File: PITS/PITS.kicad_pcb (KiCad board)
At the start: 2 copper layers, 65 x 30 mm, 55 parts, among them P1 CONN_02X20, P10 I2C, P11 I2C, P12 I2C, P13 I2C, P14 BATT, P2 BNC, P3 BNC, P4 BNC, P5 BNC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

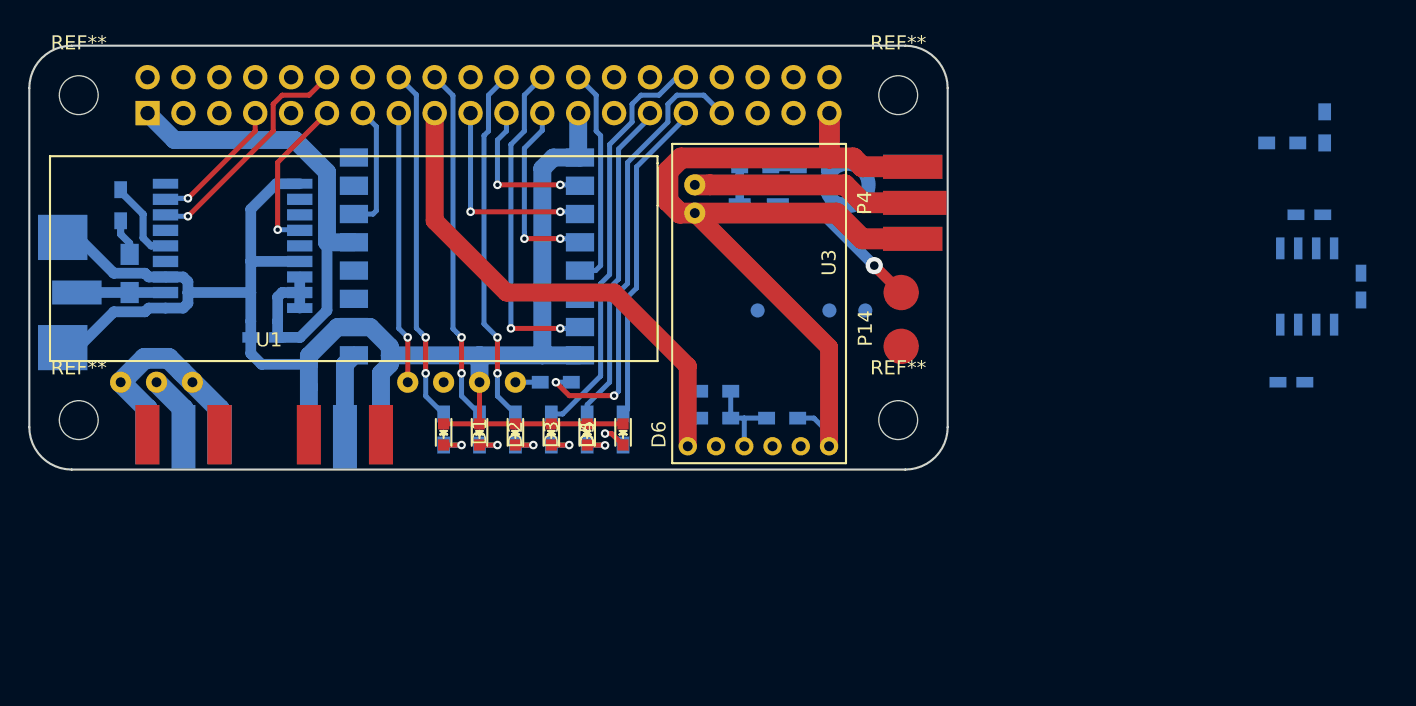
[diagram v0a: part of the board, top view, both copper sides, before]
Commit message: ADC, BME280 and power switch
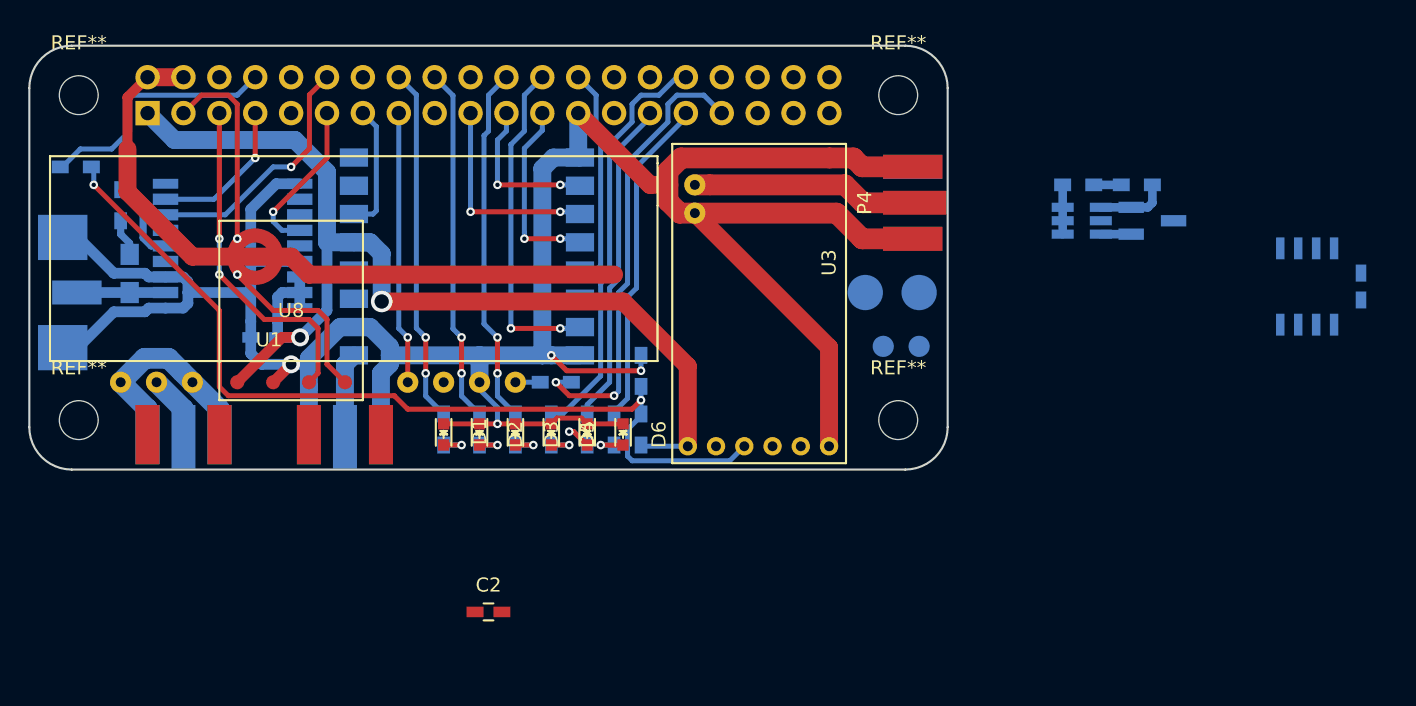
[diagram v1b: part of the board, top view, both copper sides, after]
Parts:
- removed C4: 100n, Capacitors_SMD:C_0603_HandSoldering
- removed R12, R13: 10k, Resistors_SMD:R_0603_HandSoldering
- added P6: Batt, Connectors:SMD_2_xsmall, B.Cu at (115.4, 70.3)
- C2, U8: moved to F.Cu
- P14: moved to B.Cu
- moved C2 64.5 mm to (87.5, 89.1)
- moved R3 48.0 mm to (58.3, 57.6)
- moved U8 44.7 mm to (69.7, 72.8), turned to 0 degrees
- moved Q1 22.9 mm to (134.5, 61.4)
- moved Q2 22.9 mm to (129.5, 61.4)
- moved R6 22.9 mm to (129.2, 58.9)
- moved R19 22.9 mm to (133.4, 58.9)
- moved R2 10.5 mm to (98.3, 72.0), turned to 90 degrees
- moved R4 5.31 mm to (98.3, 76.2), turned to 90 degrees
- moved P14 1.27 mm to (118.0, 66.5), turned to 180 degrees
- moved R23 0.64 mm to (96.4, 76.2)
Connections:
- C2 pad 2: GND -> Net-(C2-Pad2)
- P1 pad 2: +5V -> I_neg
- P1 pad 4: +5V -> I_neg
- P14 pad 1: +5V_PSU -> I_pos
- Q1 pad 1: +5V_PSU -> I_pos
- Q1 pad 3: +5V -> I_neg
- Q2 pad 5: +5V -> I_neg
- Q2 pad 6: +5V_PSU -> I_pos
- U1 pad 5: +5V -> I_neg
- U5 pad 3: +5V_PSU -> I_pos
- U7 pad 2: GND -> Net-(C2-Pad2)
- U7 pad 7: Iout -> I_pos
- U7 pad 8: GND -> I_neg
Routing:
- net /MTX2-TXD: track 6.44 -> 64.2 mm, vias 0 -> 2
- net I_neg: track 0.00 -> 48.1 mm
- net /GPIO2(SDA1): track 0.00 -> 29.3 mm, vias 0 -> 2
- net /GPIO3(SCL1): track 0.00 -> 24.1 mm, vias 0 -> 2
- net /GPIO14(TXD0): track 0.00 -> 17.8 mm
- net GND: track 201.4 -> 213.6 mm, vias 0 -> 4
- net +5V_PSU: track 11.0 -> 0.00 mm, vias 1 -> 0
- net +3V3: track 75.2 -> 81.4 mm, vias 0 -> 2
- net I_pos: track 0.00 -> 2.15 mm
- net /GPIO4: track 9.62 -> 10.7 mm
- net /GPIO18: track 16.7 -> 17.7 mm
- net /D6: track 3.37 -> 2.53 mm
- net /D5: track 2.55 -> 3.33 mm
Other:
- net class POWER: via_dia 1.2192 -> 1.524; via_drill 0.6096 -> 1.016

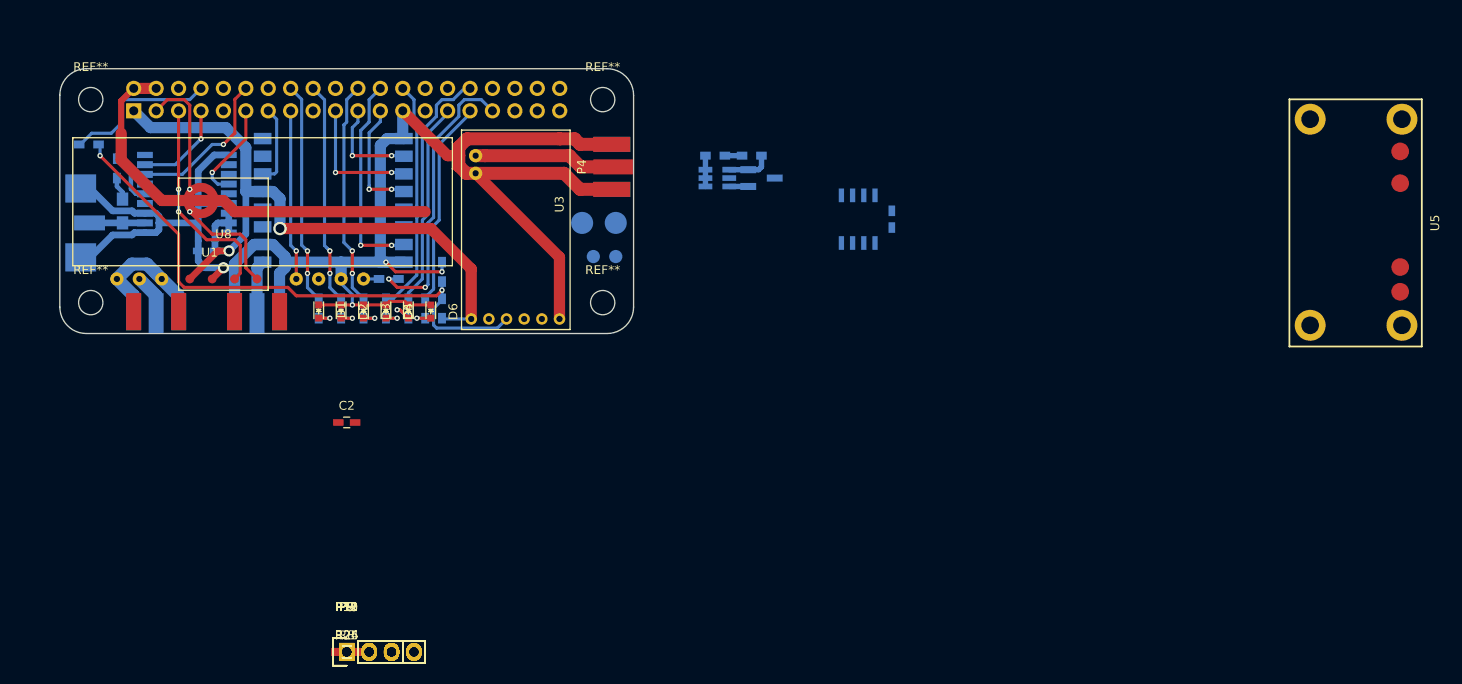
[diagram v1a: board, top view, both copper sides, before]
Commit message: Layout almost finished
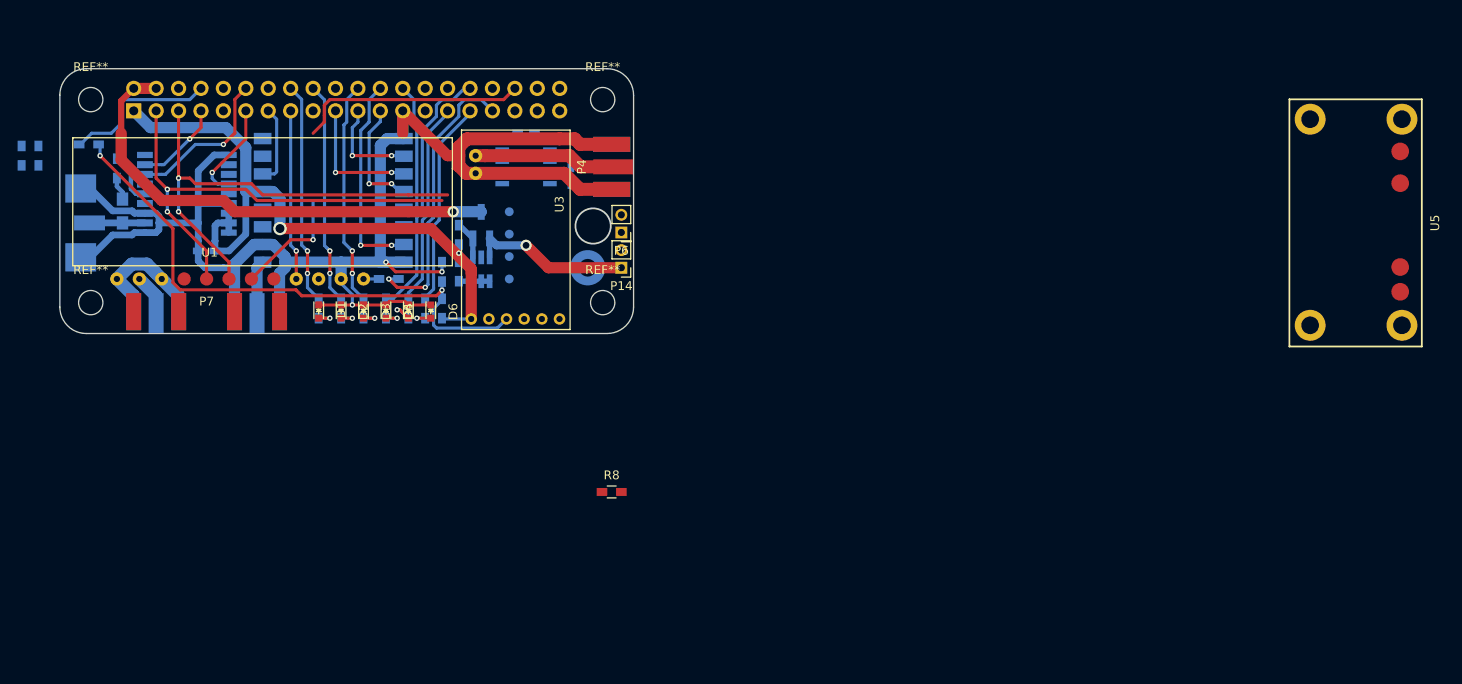
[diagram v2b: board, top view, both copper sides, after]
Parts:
- removed P10, P11, P12, P13: I2C, Socket_Strips:Socket_Strip_Straight_1x04
- removed P8, P9: 1-WIRE, Socket_Strips:Socket_Strip_Straight_1x03
- C2, R24, R25: moved to B.Cu
- P14: footprint Connectors:SMD_2_small -> Pin_Headers:Pin_Header_Straight_1x02_Pitch2.00mm; moved to F.Cu
- P6: footprint Connectors:SMD_2_xsmall -> Pin_Headers:Pin_Header_Straight_1x02_Pitch2.00mm; moved to F.Cu
- P7: value 1-WIRE -> SENSOR; footprint Socket_Strips:Socket_Strip_Straight_1x03 -> Connectors:SMD_5_xsmall
- U8: footprint RF_Modules:BME280 -> RF_Modules:BME280_edit; moved to B.Cu
- moved R24 67.2 mm to (50.7, 58.9), turned to 90 degrees
- moved R25 66.2 mm to (52.6, 58.9), turned to 90 degrees
- moved P7 46.1 mm to (69.1, 72.8)
- moved C1 42.6 mm to (107.8, 56.3), turned to 0 degrees
- moved U7 38.1 mm to (107.8, 60.1), turned to 0 degrees
- moved C2 37.8 mm to (112.9, 61.1), turned to 270 degrees
- moved U8 36.2 mm to (105.9, 72.8), turned to 90 degrees
- moved R8 35.1 mm to (117.5, 97.0)
- moved R19 34.4 mm to (100.2, 67.8), turned to 270 degrees
- moved Q1 32.2 mm to (102.7, 66.7), turned to 180 degrees
- moved R6 31.9 mm to (100.2, 72.0), turned to 90 degrees
- moved Q2 28.7 mm to (102.7, 71.7), turned to 90 degrees
- moved P14 5.12 mm to (118.6, 71.5)
- moved P6 4.19 mm to (118.6, 67.5), turned to 180 degrees
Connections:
- P7 pad 2: /GPIO4 -> /GPIO2(SDA1)
- P7 pad 3: GND -> /GPIO3(SCL1)
- R8 pad 2: /GPIO4 -> /GPIO16(CE2)
- U7 pad 1: Net-(C2-Pad1) -> I_neg
- U7 pad 2: Net-(C2-Pad2) -> I_pos
- U7 pad 7: I_pos -> Net-(C2-Pad1)
- U7 pad 8: I_neg -> Net-(C2-Pad2)
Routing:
- net /GPIO16(CE2): track 0.00 -> 39.4 mm, vias 0 -> 1
- net /GPIO3(SCL1): track 24.1 -> 52.7 mm
- net /GPIO2(SDA1): track 29.3 -> 53.1 mm
- net GND: track 213.6 -> 193.9 mm
- net I_pos: track 2.15 -> 18.5 mm, vias 0 -> 1
- net I_neg: track 48.1 -> 54.5 mm, vias 0 -> 1
- net +3V3: track 81.4 -> 75.6 mm, vias 2 -> 1
- net /GPIO4: track 10.7 -> 9.99 mm
- net Net-(Q1-Pad2): track 5.05 -> 4.36 mm

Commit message: Some cleanup
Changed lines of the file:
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@@
-    )
-  )
-  (module RF_Modules:MTX2 locked (layer F.Cu)
-    (at 101.605 58.35 270)
-    (fp_text reference U3 (at 6 -10 270) (layer F.SilkS)
-      (effects (font (size 1 1) (thickness 0.15)))
-    )
-    (fp_text value MTX2 (at 0 -10 270) (layer F.Fab)
-      (effects (font (size 1 1) (thickness 0.15)))
-    )
-    (fp_line (start -2.4 1.1) (end 20.2 1.1) (layer F.SilkS) (width 0.15))
-    (fp_line (start 20.2 1.1) (end 20.2 -11.2) (layer F.SilkS) (width 0.15))
-    (fp_line (start 20.2 -11.2) (end -2.4 -11.2) (layer F.SilkS) (width 0.15))
-    (fp_line (start -2.4 -11.2) (end -2.4 1.1) (layer F.SilkS) (width 0.15))
-    (pad 1 thru_hole circle (at 0.5 -0.5 270) (size 1.5 1.5) (drill 0.7) (layers *.Cu *.Mask)
-      (net 31 "Net-(P4-Pad1)"))
-    (pad 2 thru_hole circle (at 2.5 -0.5 270) (size 1.5 1.5) (drill 0.7) (layers *.Cu *.Mask)
-      (net 4 GND))
-    (pad 3 thru_hole circle (at 19 0 270) (size 1.3 1.3) (drill 0.7) (layers *.Cu *.Mask)
-      (net 1 +3V3))
-    (pad 4 thru_hole circle (at 19 -2 270) (size 1.3 1.3) (drill 0.7) (layers *.Cu *.Mask)
-      (net 60 "Net-(U3-Pad4)"))
-    (pad 5 thru_hole circle (at 19 -4 270) (size 1.3 1.3) (drill 0.7) (layers *.Cu *.Mask)
-      (net 42 /MTX2-TXD))
-    (pad 6 thru_hole circle (at 19 -6 270) (size 1.3 1.3) (drill 0.7) (layers *.Cu *.Mask)
-      (net 53 "Net-(U3-Pad6)"))
-    (pad 7 thru_hole circle (at 19 -8 270) (size 1.3 1.3) (drill 0.7) (layers *.Cu *.Mask)
-      (net 54 "Net-(U3-Pad7)"))
-    (pad 8 thru_hole circle (at 19 -10 270) (size 1.3 1.3) (drill 0.7) (layers *.Cu *.Mask)
-      (net 4 GND))
-    (model RF_Modules.3dshapes/MTX2.wrl
-      (at (xyz 0 0 0))
-      (scale (xyz 0.393700787 0.393700787 0.393700787))
-      (rotate (xyz 0 0 0))
     )
   )
@@
       (rotate (xyz 0 0 0))
     )
+  )
+  (module RF_Modules:MTX2 locked (layer F.Cu)
+    (at 101.605 58.35 270)
+    (fp_text reference U3 (at 6 -10 270) (layer F.SilkS)
+      (effects (font (size 1 1) (thickness 0.15)))
+    )
+    (fp_text value MTX2 (at 0 -10 270) (layer F.Fab)
+      (effects (font (size 1 1) (thickness 0.15)))
+    )
+    (fp_line (start -2.6 1.3) (end 20.4 1.3) (layer F.SilkS) (width 0.15))
+    (fp_line (start 20.4 1.3) (end 20.4 -11.4) (layer F.SilkS) (width 0.15))
+    (fp_line (start 20.4 -11.4) (end -2.6 -11.4) (layer F.SilkS) (width 0.15))
+    (fp_line (start -2.6 -11.4) (end -2.6 1.3) (layer F.SilkS) (width 0.15))
+    (pad 1 thru_hole circle (at 0.5 -0.5 270) (size 1.5 1.5) (drill 0.8) (layers *.Cu *.Mask)
+      (net 31 "Net-(P4-Pad1)"))
+    (pad 2 thru_hole circle (at 2.5 -0.5 270) (size 1.5 1.5) (drill 0.8) (layers *.Cu *.Mask)
+      (net 4 GND))
+    (pad 3 thru_hole circle (at 19 0 270) (size 1.3 1.3) (drill 0.8) (layers *.Cu *.Mask)
+      (net 1 +3V3))
+    (pad 4 thru_hole circle (at 19 -2 270) (size 1.3 1.3) (drill 0.8) (layers *.Cu *.Mask)
+      (net 60 "Net-(U3-Pad4)"))
+    (pad 5 thru_hole circle (at 19 -4 270) (size 1.3 1.3) (drill 0.8) (layers *.Cu *.Mask)
+      (net 42 /MTX2-TXD))
+    (pad 6 thru_hole circle (at 19 -6 270) (size 1.3 1.3) (drill 0.8) (layers *.Cu *.Mask)
+      (net 53 "Net-(U3-Pad6)"))
+    (pad 7 thru_hole circle (at 19 -8 270) (size 1.3 1.3) (drill 0.8) (layers *.Cu *.Mask)
+      (net 54 "Net-(U3-Pad7)"))
+    (pad 8 thru_hole circle (at 19 -10 270) (size 1.3 1.3) (drill 0.8) (layers *.Cu *.Mask)
+      (net 4 GND))
+    (model RF_Modules.3dshapes/MTX2.wrl
+      (at (xyz 0 0 0))
+      (scale (xyz 0.393700787 0.393700787 0.393700787))
+      (rotate (xyz 0 0 0))
+    )

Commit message: PCB save
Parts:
- moved U5 59.7 mm to (142.1, 65.2)
- moved R8 56.4 mm to (142.1, 46.1)
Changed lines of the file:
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@@
   )
   (module Resistors_SMD:R_0603_HandSoldering (layer F.Cu)
-    (at 117.515 96.95)
+    (at 142.11 46.15)
     (descr "Resistor SMD 0603, hand soldering")
     (tags "resistor 0603")
@@
     (model RF_Modules.3dshapes/HX1.wrl
       (at (xyz -0.19685 0.059055 0))
-      (scale (xyz 0.393701 0.393701 0.393701))
-      (rotate (xyz 0 0 0))
-    )
-  )
-  (module power:TPS61030 (layer F.Cu)
-    (at 201.8 66.47 90)
-    (fp_text reference U5 (at 0 9 90) (layer F.SilkS)
-      (effects (font (size 1 1) (thickness 0.15)))
-    )
-    (fp_text value TPS61030 (at 0 0 90) (layer F.Fab)
-      (effects (font (size 1 1) (thickness 0.15)))
-    )
-    (fp_line (start 14 7.5) (end -14 7.5) (layer F.SilkS) (width 0.2))
-    (fp_line (start 14 -7.5) (end 14 7.5) (layer F.SilkS) (width 0.2))
-    (fp_line (start -14 -7.5) (end 14 -7.5) (layer F.SilkS) (width 0.2))
-    (fp_line (start -14 7.5) (end -14 -7.5) (layer F.SilkS) (width 0.2))
-    (pad 1 smd circle (at -7.8 5.05 90) (size 2 2) (layers F.Cu F.Paste F.Mask)
-      (net 27 +BATT))
-    (pad 2 smd circle (at -5 5.05 90) (size 2 2) (layers F.Cu F.Paste F.Mask)
-      (net 4 GND))
-    (pad 2 smd circle (at 4.5 5.05 90) (size 2 2) (layers F.Cu F.Paste F.Mask)
-      (net 4 GND))
-    (pad 3 smd circle (at 8.1 5.05 90) (size 2 2) (layers F.Cu F.Paste F.Mask)
-      (net 65 I_pos))
-    (pad 4 thru_hole circle (at -11.6 5.25 90) (size 3.5 3.5) (drill 2) (layers B.Cu B.Mask))
-    (pad 4 thru_hole circle (at -11.6 -5.15 90) (size 3.5 3.5) (drill 2) (layers B.Cu B.Mask))
-    (pad 4 thru_hole circle (at 11.75 -5.15 90) (size 3.5 3.5) (drill 2) (layers B.Cu B.Mask))
-    (pad 4 thru_hole circle (at 11.75 5.25 90) (size 3.5 3.5) (drill 2) (layers B.Cu B.Mask))
-    (model power.3dshapes/TPS61030-1.wrl
-      (at (xyz -0.551181 -0.295276 0.28))
       (scale (xyz 0.393701 0.393701 0.393701))
       (rotate (xyz 0 0 0))
@@
       (rotate (xyz 0 0 0))
     )
+  )
+  (module power:TPS61030 (layer F.Cu)
+    (at 142.11 65.2 90)
+    (fp_text reference U5 (at 0 9 90) (layer F.SilkS)
+      (effects (font (size 1 1) (thickness 0.15)))
+    )
+    (fp_text value TPS61030 (at 0 0 90) (layer F.Fab)
+      (effects (font (size 1 1) (thickness 0.15)))
+    )
+    (fp_line (start 14 7.5) (end -14 7.5) (layer F.SilkS) (width 0.2))
+    (fp_line (start 14 -7.5) (end 14 7.5) (layer F.SilkS) (width 0.2))
+    (fp_line (start -14 -7.5) (end 14 -7.5) (layer F.SilkS) (width 0.2))
+    (fp_line (start -14 7.5) (end -14 -7.5) (layer F.SilkS) (width 0.2))
+    (pad 1 smd circle (at -7.8 5.05 90) (size 2 2) (layers F.Cu F.Paste F.Mask)
+      (net 27 +BATT))
+    (pad 2 smd circle (at -5 5.05 90) (size 2 2) (layers F.Cu F.Paste F.Mask)
+      (net 4 GND))
+    (pad 2 smd circle (at 4.5 5.05 90) (size 2 2) (layers F.Cu F.Paste F.Mask)
+      (net 4 GND))
+    (pad 3 smd circle (at 8.1 5.05 90) (size 2 2) (layers F.Cu F.Paste F.Mask)
+      (net 65 I_pos))
+    (pad 4 thru_hole circle (at -11.6 5.25 90) (size 3.5 3.5) (drill 2) (layers B.Cu B.Mask))
+    (pad 4 thru_hole circle (at -11.6 -5.15 90) (size 3.5 3.5) (drill 2) (layers B.Cu B.Mask))
+    (pad 4 thru_hole circle (at 11.75 -5.15 90) (size 3.5 3.5) (drill 2) (layers B.Cu B.Mask))
+    (pad 4 thru_hole circle (at 11.75 5.25 90) (size 3.5 3.5) (drill 2) (layers B.Cu B.Mask))
+    (model power.3dshapes/TPS61030.wrl
+      (at (xyz -0.551181 -0.295276 0))
+      (scale (xyz 0.393701 0.393701 0.393701))
+      (rotate (xyz 0 0 0))
+    )
